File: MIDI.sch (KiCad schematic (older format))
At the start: 13 parts

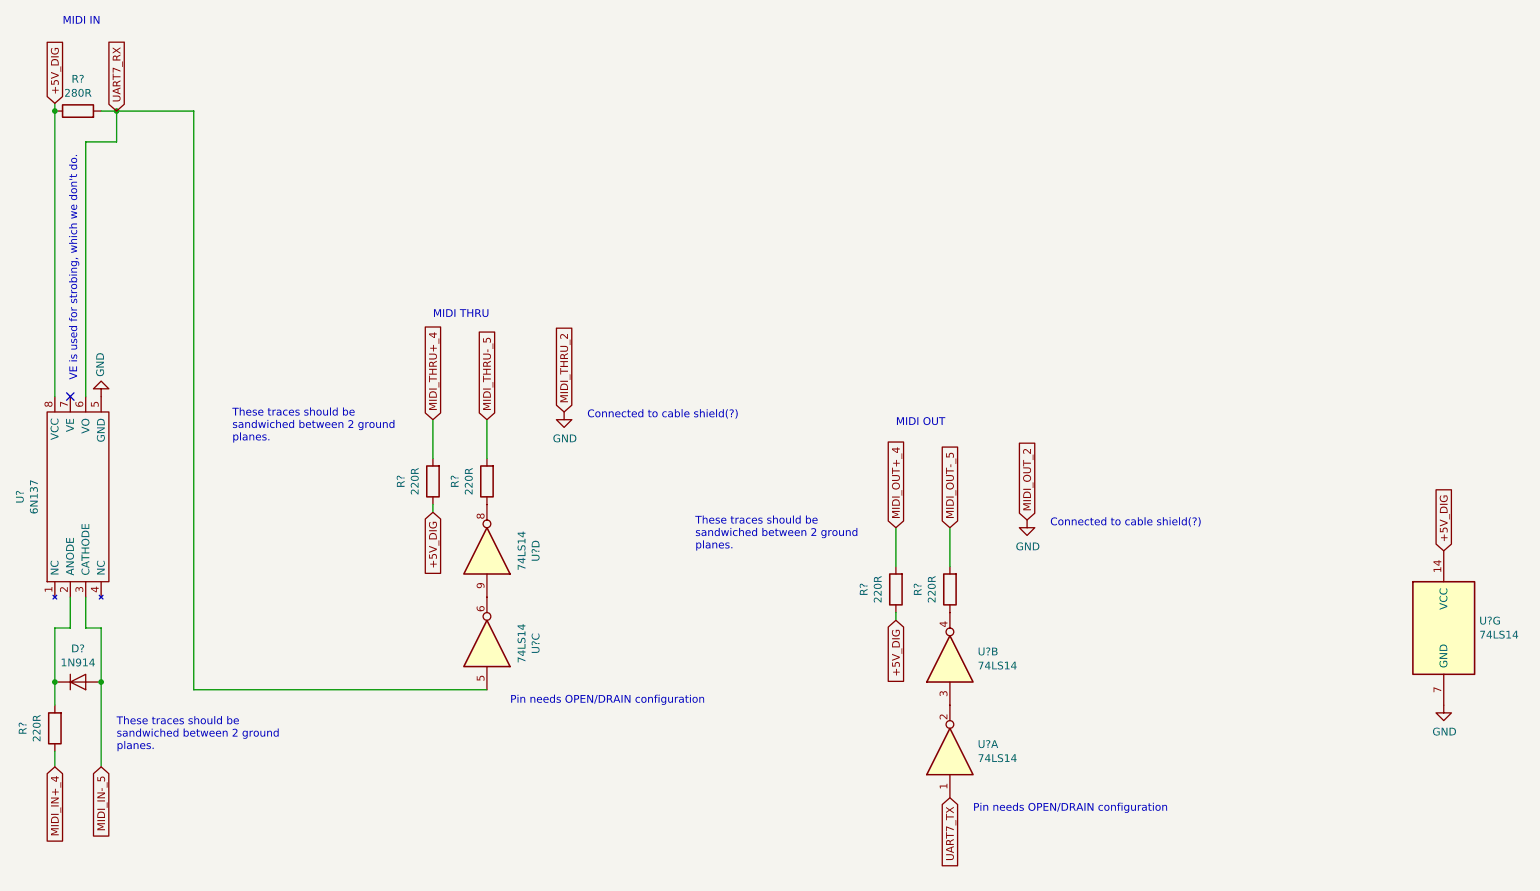
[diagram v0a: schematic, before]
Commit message: First proposed pin layout of SODIMM connector
Will need to add GPIO / ADC pins as needed, but let's wait to see if we don't
need to use more pins.

Double-checked and fixed CODEC and MCU's power supply.
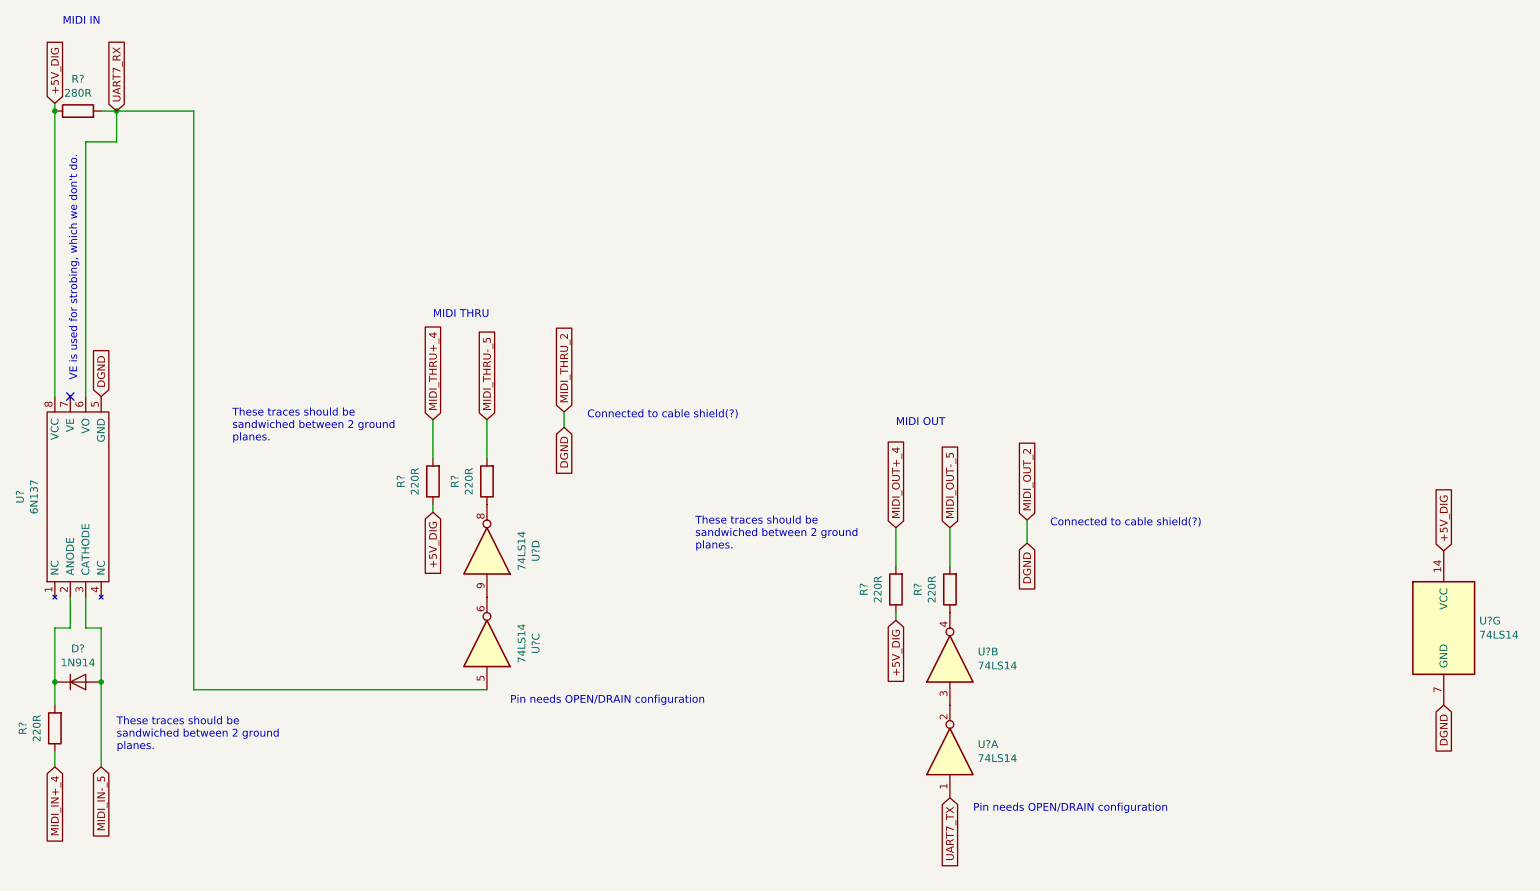
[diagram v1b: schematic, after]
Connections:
- net GND renamed DGND
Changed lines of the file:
@@
 $Descr A4 11693 8268
 encoding utf-8
-Sheet 10 12
+Sheet 10 13
 Title ""
 Date ""
@@
 	1    0    0    -1
 $EndComp
-$Comp
-L power:GND #PWR?
-U 1 1 5D016F67
-P 10250 5100
-F 0 "#PWR?" H 10250 4850 50  0001 C CNN
-F 1 "GND" H 10255 4927 50  0000 C CNN
-F 2 "" H 10250 5100 50  0001 C CNN
-F 3 "" H 10250 5100 50  0001 C CNN
-	1    10250 5100
-	1    0    0    -1
-$EndComp
 Text GLabel 10250 4100 1    50   Input ~ 0
 +5V_DIG
@@
 Text Notes 1400 3000 1    50   ~ 0
 VE is used for strobing, which we don't do.
-$Comp
-L power:GND #PWR?
-U 1 1 5D01CFC9
-P 1550 3100
-F 0 "#PWR?" H 1550 2850 50  0001 C CNN
-F 1 "GND" V 1555 2972 50  0000 R CNN
-F 2 "" H 1550 3100 50  0001 C CNN
-F 3 "" H 1550 3100 50  0001 C CNN
-	1    1550 3100
-	-1   0    0    1
-$EndComp
 Wire Wire Line
 	1250 1200 1250 1250
@@
 Text GLabel 7550 3900 1    50   Input ~ 0
 MIDI_OUT_2
-$Comp
-L power:GND #PWR?
-U 1 1 5D01FABF
-P 7550 3900
-F 0 "#PWR?" H 7550 3650 50  0001 C CNN
-F 1 "GND" H 7555 3727 50  0000 C CNN
-F 2 "" H 7550 3900 50  0001 C CNN
-F 3 "" H 7550 3900 50  0001 C CNN
-	1    7550 3900
-	1    0    0    -1
-$EndComp
 Text Notes 7700 3950 0    50   ~ 0
 Connected to cable shield(?)
@@
 Text GLabel 4550 3200 1    50   Input ~ 0
 MIDI_THRU_2
-$Comp
-L power:GND #PWR?
-U 1 1 5D0214CE
-P 4550 3200
-F 0 "#PWR?" H 4550 2950 50  0001 C CNN
-F 1 "GND" H 4555 3027 50  0000 C CNN
-F 2 "" H 4550 3200 50  0001 C CNN
-F 3 "" H 4550 3200 50  0001 C CNN
-	1    4550 3200
-	1    0    0    -1
-$EndComp
 Text Notes 4700 3250 0    50   ~ 0
 Connected to cable shield(?)
@@
 Wire Wire Line
 	1650 1250 2150 1250
+Text GLabel 1550 3100 1    50   Input ~ 0
+DGND
+Text GLabel 10250 5100 3    50   Input ~ 0
+DGND
+Text GLabel 7550 4050 3    50   Input ~ 0
+DGND
+Wire Wire Line
+	7550 3900 7550 4050
+Text GLabel 4550 3300 3    50   Input ~ 0
+DGND
+Wire Wire Line
+	4550 3300 4550 3200
 $EndSCHEMATC
